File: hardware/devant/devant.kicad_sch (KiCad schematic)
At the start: 0 parts

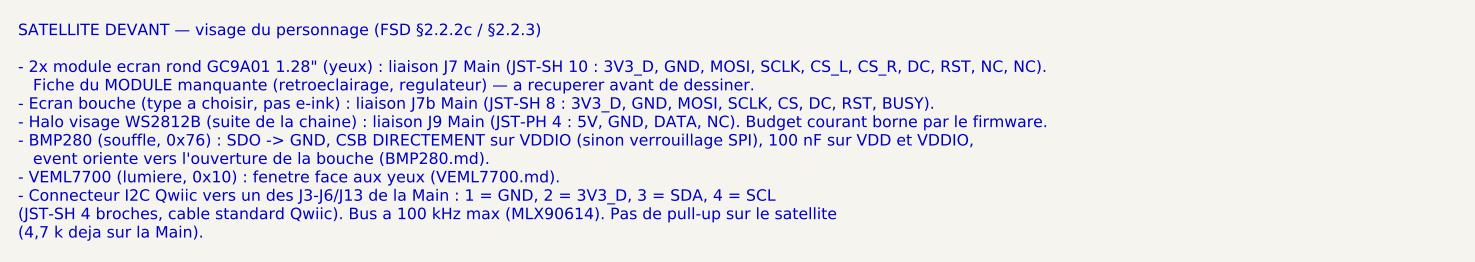
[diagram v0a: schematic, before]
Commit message: hardware+docs: CAP1298 retenu pour le tactile de Cote 2, BOM de reference corrigee (H8)
- Cote 2 : CAP1298-1-SL-TR (C2652072, 8 touches, 0x28 fixe) remplace le MTCH2120
  (aucun stock) ; proximite de Cote 3 en suspens (pas de second CAP12xx).
- BOM : U11 = LSM6DSOXTR, doublon U21 retire, filtre DAC 470 ohm + 2,2 nF C0G,
  TMAG5273A1 (C3716049), U10 SOT-23-6, ecran bouche a choisir, LCSC de D1/Q1/Q2
  dans la bonne colonne, ST25DV et haut-parleur ajoutes.
- docs/pcb/02-bom-lcsc.csv (perimee) supprimee : une seule BOM.
- FSD, RESTE-A-FAIRE, syntheses et cartouches satellites alignes.
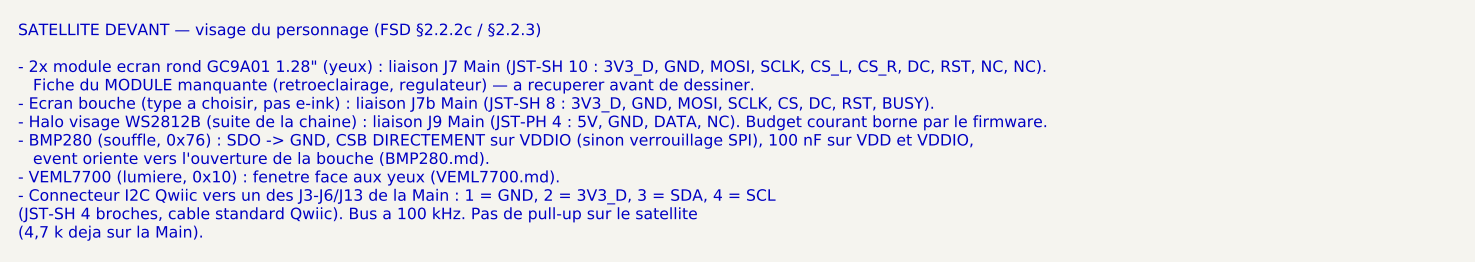
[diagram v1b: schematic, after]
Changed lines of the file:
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@@
 	(generator_version "10.0")
 	(paper "A4")
-	(text "SATELLITE DEVANT — visage du personnage (FSD §2.2.2c / §2.2.3)\n\n- 2x module ecran rond GC9A01 1.28\" (yeux) : liaison J7 Main (JST-SH 10 : 3V3_D, GND, MOSI, SCLK, CS_L, CS_R, DC, RST, NC, NC).\n   Fiche du MODULE manquante (retroeclairage, regulateur) — a recuperer avant de dessiner.\n- Ecran bouche (type a choisir, pas e-ink) : liaison J7b Main (JST-SH 8 : 3V3_D, GND, MOSI, SCLK, CS, DC, RST, BUSY).\n- Halo visage WS2812B (suite de la chaine) : liaison J9 Main (JST-PH 4 : 5V, GND, DATA, NC). Budget courant borne par le firmware.\n- BMP280 (souffle, 0x76) : SDO -> GND, CSB DIRECTEMENT sur VDDIO (sinon verrouillage SPI), 100 nF sur VDD et VDDIO,\n   event oriente vers l'ouverture de la bouche (BMP280.md).\n- VEML7700 (lumiere, 0x10) : fenetre face aux yeux (VEML7700.md).\n- Connecteur I2C Qwiic vers un des J3-J6/J13 de la Main : 1 = GND, 2 = 3V3_D, 3 = SDA, 4 = SCL\n(JST-SH 4 broches, cable standard Qwiic). Bus a 100 kHz max (MLX90614). Pas de pull-up sur le satellite\n(4,7 k deja sur la Main)."
+	(text "SATELLITE DEVANT — visage du personnage (FSD §2.2.2c / §2.2.3)\n\n- 2x module ecran rond GC9A01 1.28\" (yeux) : liaison J7 Main (JST-SH 10 : 3V3_D, GND, MOSI, SCLK, CS_L, CS_R, DC, RST, NC, NC).\n   Fiche du MODULE manquante (retroeclairage, regulateur) — a recuperer avant de dessiner.\n- Ecran bouche (type a choisir, pas e-ink) : liaison J7b Main (JST-SH 8 : 3V3_D, GND, MOSI, SCLK, CS, DC, RST, BUSY).\n- Halo visage WS2812B (suite de la chaine) : liaison J9 Main (JST-PH 4 : 5V, GND, DATA, NC). Budget courant borne par le firmware.\n- BMP280 (souffle, 0x76) : SDO -> GND, CSB DIRECTEMENT sur VDDIO (sinon verrouillage SPI), 100 nF sur VDD et VDDIO,\n   event oriente vers l'ouverture de la bouche (BMP280.md).\n- VEML7700 (lumiere, 0x10) : fenetre face aux yeux (VEML7700.md).\n- Connecteur I2C Qwiic vers un des J3-J6/J13 de la Main : 1 = GND, 2 = 3V3_D, 3 = SDA, 4 = SCL\n(JST-SH 4 broches, cable standard Qwiic). Bus a 100 kHz. Pas de pull-up sur le satellite\n(4,7 k deja sur la Main)."
 		(exclude_from_sim no)
 		(at 20.32 142.24 0)
